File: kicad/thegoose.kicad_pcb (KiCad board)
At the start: 6 copper layers, 88.5 x 47 mm, 190 parts, among them J1 USB_C_Receptacle_USB2.0_16P, J11 Balance, J12 LED stick, J3 XT30UPB-M, J4 USB-A host, J5 IO 3x6 RA, Q1 AO4407A, Q2 80N03F, Q3 80N03F, SW1 Power, SW2 BOOT, U1 DRV8848, U10 RP2354A, U11 SRV05-4, U12 SY6280AAC, U13 BQ7791501, U14 74AHCT1G125, U2 DRV8848, U3 DRV8848, U4 AP64500SP-13, U5 CH224A, U6 SRV05-4, U7 BQ25798, U8 HT7550-1, U9 XC6206P332MR, Y1 12MHz

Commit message: Split into brain + smart pack, and support 2S packs
Brain/pack split: charging, protection and the fuse move off the brain
into a separate smart pack board (kicad-pack/goosepack), with its own
USB-C charging port. The brain drops to 4 layers, loses the charger,
PD sink, protector and SY6280, and swaps the DRV8848s for DRV8871s.

2S support on the brain:
- DRV8871 -> DRV8251A (same HSOP-8 footprint, 4.5-48 V VM). Shared VREF
  divider R107/R108/C81 from +3V3 (2.53 V) and 1.18k IPROPI resistors
  keep the 1.36 A limit.
- Q1 gate divider 27k/10k -> 47k/4.7k for -5.1 V drive at an empty 2S
  pack; C71 4.7n -> 10n to keep the ~70 us soft start.

New 2S pack variant (kicad-pack-2s/goosepack2s): BQ25798 PROG 8.2k
(2S, 750 kHz), ILIM R33 18k (~0.42 A charge), ABLIC S-8252AAH protector
in place of the BQ7791501, two HY2213-BB3A balancers with AO3400A and
47R 2512 bleed resistors, 3-pin XH balance header, R94 4.7k for trip
recovery. fab.py builds it with --board pack2s.

Several new parts still need LCSC numbers; fab.py flags each one.

Co-Authored-By: Claude Opus 5.5 <noreply@anthropic.com>
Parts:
- removed C13, C2, C9: 2.2uF, Capacitor_SMD:C_0603_1608Metric
- removed C17: 1uF, Capacitor_SMD:C_0603_1608Metric
- removed C18, C19: 47nF, Capacitor_SMD:C_0603_1608Metric
- removed C20, C21, C23, C24, C25, C27, C28, C29, C30, C31, C33, C34, C70: 10uF, Capacitor_SMD:C_0805_2012Metric
- removed C22, C26, C32, C60, C68: 100nF, Capacitor_SMD:C_0402_1005Metric
- removed C35: 4.7uF, Capacitor_SMD:C_0603_1608Metric
- removed C36: 1nF, Capacitor_SMD:C_0402_1005Metric
- removed C58, C62, C63, C64, C65, C66, C67: 1uF, Capacitor_SMD:C_0402_1005Metric
- removed D1: SMBJ20A, Diode_SMD:D_SMB
- removed F1: 15A fast, Fuse:Fuse_Littelfuse-NANO2-451_453
- removed J11: Balance, Connector_JST:JST_XH_B4B-XH-A_1x04_P2.50mm_Vertical
- removed L2: 2.2uH, Inductor_SMD:L_Changjiang_FNR4030S
- removed LED1: green, hexy:LED_Everlight_27-21_SideView
- removed Q2, Q3: 80N03F, Package_TO_SOT_SMD:TDSON-8-1
- removed R29, R31, R78: 6.8k, Resistor_SMD:R_0402_1005Metric
- removed R30, R62, R63, R64, R65, R68, R69: 100, Resistor_SMD:R_0402_1005Metric
- removed R32, R50, R76: 100k, Resistor_SMD:R_0402_1005Metric
- removed R33: 33k, Resistor_SMD:R_0402_1005Metric
- removed R34: 5.23k, Resistor_SMD:R_0402_1005Metric
- removed R35: 30.1k, Resistor_SMD:R_0402_1005Metric
- removed R36: 2.2k, Resistor_SMD:R_0402_1005Metric
- removed R37, R38, R39, R54, R75, R77, R79, R81, R85, R89, R93: 10k, Resistor_SMD:R_0402_1005Metric
- removed R61, R72: 1k, Resistor_SMD:R_0402_1005Metric
- removed R66, R67: 5m, Resistor_SMD:R_2512_6332Metric
- removed R70: 4.7k, Resistor_SMD:R_0402_1005Metric
- removed R71, R73: 1M, Resistor_SMD:R_0402_1005Metric
- removed R74: 470k, Resistor_SMD:R_0402_1005Metric
- removed R80: 330, Resistor_SMD:R_0402_1005Metric
- removed R82, R83, R86, R87, R90, R91: 0.15, Resistor_SMD:R_1206_3216Metric
- removed R84, R88, R92: 15k, Resistor_SMD:R_0402_1005Metric
- removed TH1: 10k B3434, Resistor_SMD:R_0603_1608Metric
- removed U12: SY6280AAC, Package_TO_SOT_SMD:SOT-23-5
- removed U13: BQ7791501, Package_SO:TSSOP-24_4.4x7.8mm_P0.65mm
- removed U5: CH224A, Package_SO:SSOP-10-1EP_3.9x4.9mm_P1mm_EP2.1x3.3mm
- removed U7: BQ25798, Package_DFN_QFN:Texas_RQM0029A_VQFN-29_4x4mm_P0.4mm
- added C73: 10uF, Capacitor_SMD:C_0805_2012Metric, F.Cu at (163.6, 122.9)
- added C74: 100nF, Capacitor_SMD:C_0402_1005Metric, F.Cu at (163.3, 121.0)
- added C75: 10uF, Capacitor_SMD:C_0805_2012Metric, F.Cu at (166.4, 121.5)
- added C76: 100nF, Capacitor_SMD:C_0805_2012Metric, F.Cu at (168.5, 121.5)
- added C77: 10uF, Capacitor_SMD:C_0805_2012Metric, F.Cu at (166.4, 138.5)
- added C78: 100nF, Capacitor_SMD:C_0805_2012Metric, F.Cu at (168.5, 138.5)
- added C79: 10uF, Capacitor_SMD:C_0805_2012Metric, F.Cu at (132.0, 108.0)
- added C80: 100nF, Capacitor_SMD:C_0805_2012Metric, F.Cu at (134.0, 108.0)
- added C81: 100nF, Capacitor_SMD:C_0402_1005Metric, F.Cu at (148.0, 152.0)
- added F2: 0.5A hold, Fuse:Fuse_1206_3216Metric, F.Cu at (163.5, 134.0)
- added R100: 5.1k, Resistor_SMD:R_0402_1005Metric, F.Cu at (135.8, 109.8)
- added R101: 1.18k, Resistor_SMD:R_0402_1005Metric, F.Cu at (167.5, 116.2)
- added R102: 1.18k, Resistor_SMD:R_0402_1005Metric, F.Cu at (167.5, 124.7)
- added R103: 1.18k, Resistor_SMD:R_0402_1005Metric, F.Cu at (166.4, 131.0)
- added R104: 1.18k, Resistor_SMD:R_0402_1005Metric, F.Cu at (167.5, 141.7)
- added R105: 1.18k, Resistor_SMD:R_0402_1005Metric, F.Cu at (121.6, 108.7)
- added R106: 1.18k, Resistor_SMD:R_0402_1005Metric, F.Cu at (132.5, 111.8)
- added R107: 10k, Resistor_SMD:R_0402_1005Metric, F.Cu at (140.0, 152.0)
- added R108: 33k, Resistor_SMD:R_0402_1005Metric, F.Cu at (144.0, 152.0)
- added R99: 5.1k, Resistor_SMD:R_0402_1005Metric, F.Cu at (137.2, 109.8)
- added U15: DRV8251A, Package_SO:Texas_HTSOP-8-1EP_3.9x4.9mm_P1.27mm_EP2.95x4.9mm_Mask2.4x3.1mm_ThermalVias, F.Cu at (174.2, 121.5)
- added U16: DRV8251A, Package_SO:Texas_HTSOP-8-1EP_3.9x4.9mm_P1.27mm_EP2.95x4.9mm_Mask2.4x3.1mm_ThermalVias, F.Cu at (174.2, 138.5)
- added U17: DRV8251A, Package_SO:Texas_HTSOP-8-1EP_3.9x4.9mm_P1.27mm_EP2.95x4.9mm_Mask2.4x3.1mm_ThermalVias, F.Cu at (126.5, 109.5)
- C71: value 4.7nF -> 10nF
- R40: value 27k -> 47k
- R41: value 10k -> 4.7k
- U1, U2, U3: value DRV8848 -> DRV8251A; footprint Package_SO:TSSOP-16-1EP_4.4x5mm_P0.65mm -> Package_SO:Texas_HTSOP-8-1EP_3.9x4.9mm_P1.27mm_EP2.95x4.9mm_Mask2.4x3.1mm_ThermalVias
- moved C6 14.5 mm to (167.4, 127.3)
- moved U2 6.89 mm to (174.2, 130.0), turned to 0 degrees
- moved C3 5.91 mm to (166.4, 113.0), turned to 90 degrees
- moved U1 5.69 mm to (174.2, 113.0), turned to 0 degrees
- moved C7 4.90 mm to (168.5, 131.0)
- moved C4 4.70 mm to (168.5, 113.0)
- moved U3 0.94 mm to (114.2, 110.5)
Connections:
- C72 pad 1: VBAT -> PACK+
- J1 pad A5: Net-(J1-CC1) -> /Power/CC1
- J1 pad B5: Net-(J1-CC2) -> /Power/CC2
- J3 pad 1: /Power & charging/BAT_N -> GND
- J3 pad 2: /Power & charging/PACK+ -> PACK+
- M1 pad 1: Net-(M1-OUT1) -> /Motor drivers/U1_OUT1
- M1 pad 2: Net-(M1-OUT2) -> /Motor drivers/U1_OUT2
- M2 pad 1: Net-(M2-OUT1) -> /Motor drivers/U15_OUT2
- M2 pad 2: Net-(M2-OUT2) -> /Motor drivers/U15_OUT1
- M3 pad 1: Net-(M3-OUT1) -> /Motor drivers/U2_OUT1
- M3 pad 2: Net-(M3-OUT2) -> /Motor drivers/U2_OUT2
- M4 pad 1: Net-(M4-OUT1) -> /Motor drivers/U16_OUT2
- M4 pad 2: Net-(M4-OUT2) -> /Motor drivers/U16_OUT1
- M5 pad 1: Net-(M5-OUT1) -> /Motor drivers/U3_OUT1
- M5 pad 2: Net-(M5-OUT2) -> /Motor drivers/U3_OUT2
- M6 pad 1: Net-(M6-OUT1) -> /Motor drivers/U17_OUT2
- M6 pad 2: Net-(M6-OUT2) -> /Motor drivers/U17_OUT1
- Q1 pad 1: VBAT -> PACK+
- Q1 pad 2: VBAT -> PACK+
- Q1 pad 3: VBAT -> PACK+
- R40 pad 1: VBAT -> PACK+
- U1 pad 1: DRV_SLEEP -> /Motor drivers/U1_IPROPI
- U1 pad 2: Net-(M1-OUT1) -> GPIO5_M1B
- U1 pad 3: /Motor drivers/U1_AISEN -> GPIO4_M1A
- U1 pad 4: Net-(M1-OUT2) -> /Motor drivers/MOT_VREF
- U1 pad 5: Net-(M2-OUT1) -> VSYS
- U1 pad 6: /Motor drivers/U1_BISEN -> /Motor drivers/U1_OUT1
- U1 pad 7: Net-(M2-OUT2) -> GND
- U1 pad 8: DRV_FAULT -> /Motor drivers/U1_OUT2
- U1 pad 9: GPIO7_M2A -> GND
- U10 pad 12: I2C_SDA -> unconnected-(U10-GPIO8-Pad12)
- U10 pad 13: CHG_INT -> unconnected-(U10-GPIO9-Pad13)
- U10 pad 28: I2C_SCL -> unconnected-(U10-GPIO17-Pad28)
- U10 pad 31: DRV_FAULT -> unconnected-(U10-GPIO19-Pad31)
- U10 pad 35: DRV_SLEEP -> unconnected-(U10-GPIO23-Pad35)
- U10 pad 37: /MCU & USB/USBA_VBUS_EN -> unconnected-(U10-GPIO25-Pad37)
- U14 pad 4: Net-(R80-Pad1) -> Net-(J12-Pin_2)
- U2 pad 1: DRV_SLEEP -> /Motor drivers/U2_IPROPI
- U2 pad 2: Net-(M3-OUT1) -> GPIO1_M3B
- U2 pad 3: /Motor drivers/U2_AISEN -> GPIO0_M3A
- U2 pad 4: Net-(M3-OUT2) -> /Motor drivers/MOT_VREF
- U2 pad 5: Net-(M4-OUT1) -> VSYS
- U2 pad 6: /Motor drivers/U2_BISEN -> /Motor drivers/U2_OUT1
- U2 pad 7: Net-(M4-OUT2) -> GND
- U2 pad 8: DRV_FAULT -> /Motor drivers/U2_OUT2
- U2 pad 9: GPIO14_M4A -> GND
- U3 pad 1: DRV_SLEEP -> /Motor drivers/U3_IPROPI
- U3 pad 2: Net-(M5-OUT1) -> GPIO11_M5B
- U3 pad 3: /Motor drivers/U3_AISEN -> GPIO10_M5A
- U3 pad 4: Net-(M5-OUT2) -> /Motor drivers/MOT_VREF
- U3 pad 5: Net-(M6-OUT1) -> VSYS
- U3 pad 6: /Motor drivers/U3_BISEN -> /Motor drivers/U3_OUT1
- U3 pad 7: Net-(M6-OUT2) -> GND
- U3 pad 8: DRV_FAULT -> /Motor drivers/U3_OUT2
- U3 pad 9: GPIO13_M6A -> GND
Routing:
- removed copper zone on In3.Cu, net GND
- removed copper zone on In4.Cu, net GND
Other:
- copper layers 6 -> 4
- board text removed: "BAL"
- board text removed: "CHG"
- board text removed: "CHG LED1: side view, lens 0.2 mm behind the top edge at board x 35.83, centre about 0.3 mm above the board; wall hole 1.5 mm"

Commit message: Fill in LCSC numbers, swap to stocked parts, tidy the new schematic parts
- LCSC numbers from JLC's 2026-10-19 in-stock catalog for every new part
  except the DRV8251A, which JLC doesn't stock (Global Sourcing or consign).
- 2S protector S-8252AAH -> HY2120-LB (C168778): pin-for-pin the same,
  OV 4.25 V / UV 2.80 V, stocked at JLC. R94 trip recovery still holds.
- IPROPI R101-R106 1.18k (2,341 in stock) -> 1.2k preferred (C25862),
  so the motor limit is 1.34 A.
- Fix the 2S pack board's footprint-symbol links (paths were dropped in
  the previous commit); both boards now link every footprint correctly.
- Move the VREF divider and the balancer block into clear space and
  rewrite the stale DRV8871/BQ7791501 notes on the motor and 2S sheets.

Co-Authored-By: Claude Opus 5.5 <noreply@anthropic.com>
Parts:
- R101, R102, R103, R104, R105, R106: value 1.18k -> 1.2k

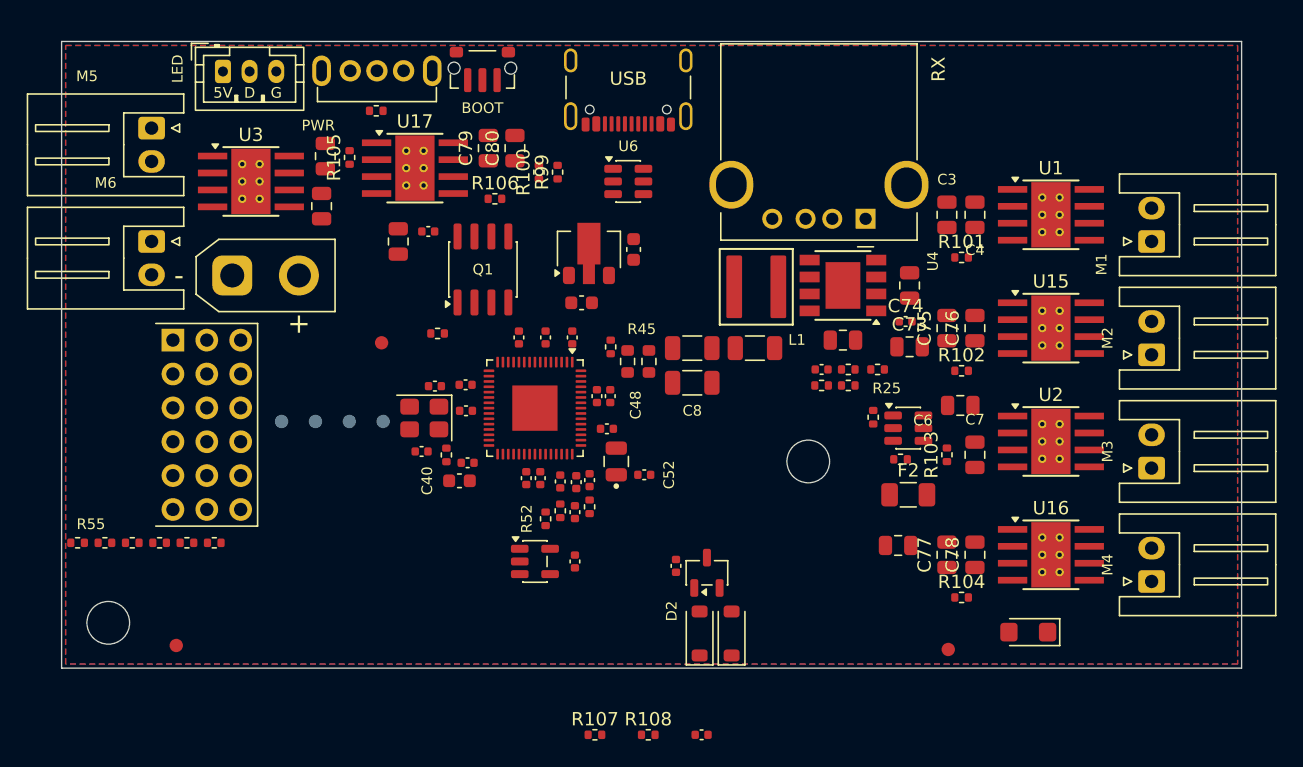
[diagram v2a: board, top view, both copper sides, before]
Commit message: Swap J3 to a horizontal XT30 and compact the brain to 78 x 46.5 mm
- J3: XT30PW-M30.G.Y (C431092) on Connector_AMASS:AMASS_XT30PW-M
  horizontal, bottom edge, mouth out through the wall. Pin 1 PACK-/GND,
  pin 2 PACK+. Hole pattern checked against the Amass drawing.
- Placement compacted from 88.5 x 47 mm to 78 x 46.5 mm (-532.5 mm2,
  -12.8 %; 10.5 mm shorter). Blocks moved as units; edge connectors stay
  on their walls; buck loop and driver-beside-connector kept.
- R107/R108/C81 placed; Edge.Cuts redrawn with 2 mm corners; mounting
  holes, fiducials, GND pours and USB rule areas moved to match.
- Stale pack-envelope and vertical-XT30 fab notes removed or rewritten.
- README/PARTS: new size, placement summary, box = outline + 5 mm.

DRC: no clearance or courtyard errors, no parts outside the outline.

Co-Authored-By: Claude Opus 5.5 <noreply@anthropic.com>
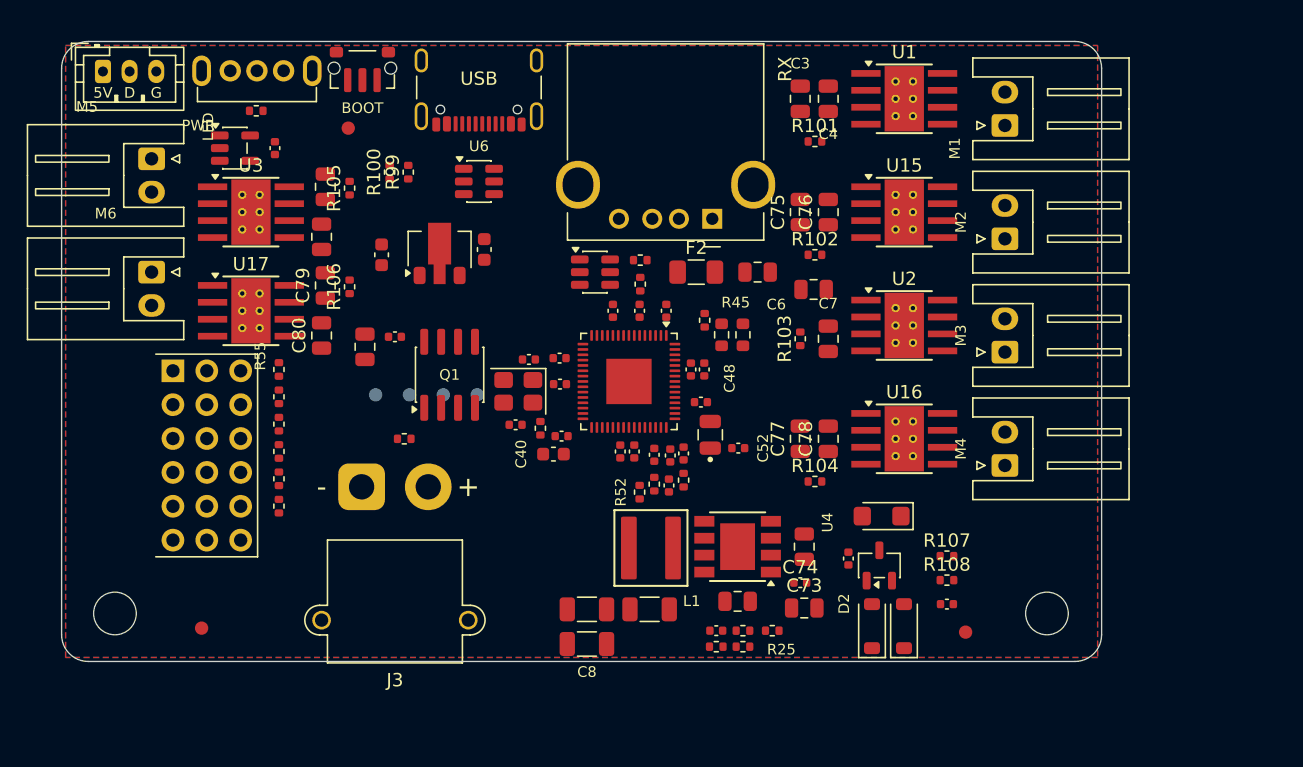
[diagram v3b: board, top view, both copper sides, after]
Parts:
- J3: value XT30UPB-M -> XT30PW-M; footprint hexy:AMASS_XT30UPB-M_1x02_P5.0mm_Vertical_EasyEDA3D -> Connector_AMASS:AMASS_XT30PW-M_1x02_P2.50mm_Horizontal
- moved C69 38.3 mm to (116.0, 108.0)
- moved U14 38.3 mm to (113.0, 108.0)
- moved R107 29.6 mm to (166.4, 138.6)
- moved G*** 26.8 mm to (147.0, 140.5)
- moved U11 26.3 mm to (140.0, 117.3)
- moved R108 25.2 mm to (166.4, 140.4)
- moved R49 23.5 mm to (143.4, 118.2), turned to -90 degrees
- moved F2 23.1 mm to (147.6, 117.3)
- moved C59 23.1 mm to (152.2, 117.3)
- moved REF** 21.2 mm to (173.9, 142.9)
- moved R25 21.1 mm to (153.3, 144.2)
- moved C12 21.1 mm to (144.1, 142.6)
- moved C14 21.1 mm to (150.7, 142.0)
- moved C16 21.1 mm to (149.1, 144.2)
- moved C5 21.1 mm to (139.4, 142.6)
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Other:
- board size 88.5 x 47 mm -> 78 x 46.5 mm
- board text added: "J3 XT30PW-M (male, horizontal) on the bottom edge: the pack's XT30U-F lead plugs in through the bottom wall. Pin 1 PACK- (GND), pin 2 PACK+."
- board text removed: "J3 XT30UPB-M (male, vertical): the pack's XT30U-F plugs in from above; mated + 16 AWG bend 22.1-24.1 mm vs 23.4 under the face (enclosure open item)"
- board text removed: "PACK: Ovonic 80C 3S 450 mAh (standard), envelope 46.5 x 25 x 21 mm (listed 44.1-46 x 24.2-24.7 x 20.3-20.5)"
- board text removed: "mounting hole under the pack: low-profile or nylon wafer head (< 1.5 mm); barrier sheet + foam between pack and board"
- board text removed: "on top of the board, 2.4 mm above it (parts under it <= 1.6 mm, barrier + foam between); leads exit at the left end"

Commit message: Compact the brain further to 73.4 x 43 mm (option B), no mounting holes
- Driver caps and IPROPI resistors moved into a row under each driver,
  next to its VM pin; the motor column moves 4.6 mm left.
- MCU and buck blocks stacked directly under J4; the USB-A strip
  (U11, R48, R49, F2, C59) and the 3.3 V rail (U9, C39, D2, D3) share
  the bottom-right corner. USB-A fan-out rule area moved with U11.
- D4, C15, the VREF divider and FID2 in the column beside J3.
- M3 mounting holes removed; the case holds the board, with a rib
  behind J3 for the plug force.
- 1,003 mm2 (24 %) smaller than the original 88.5 x 47 mm.

DRC: no clearance or courtyard errors, no parts outside the outline,
schematic parity clean.

Co-Authored-By: Claude Opus 5.5 <noreply@anthropic.com>
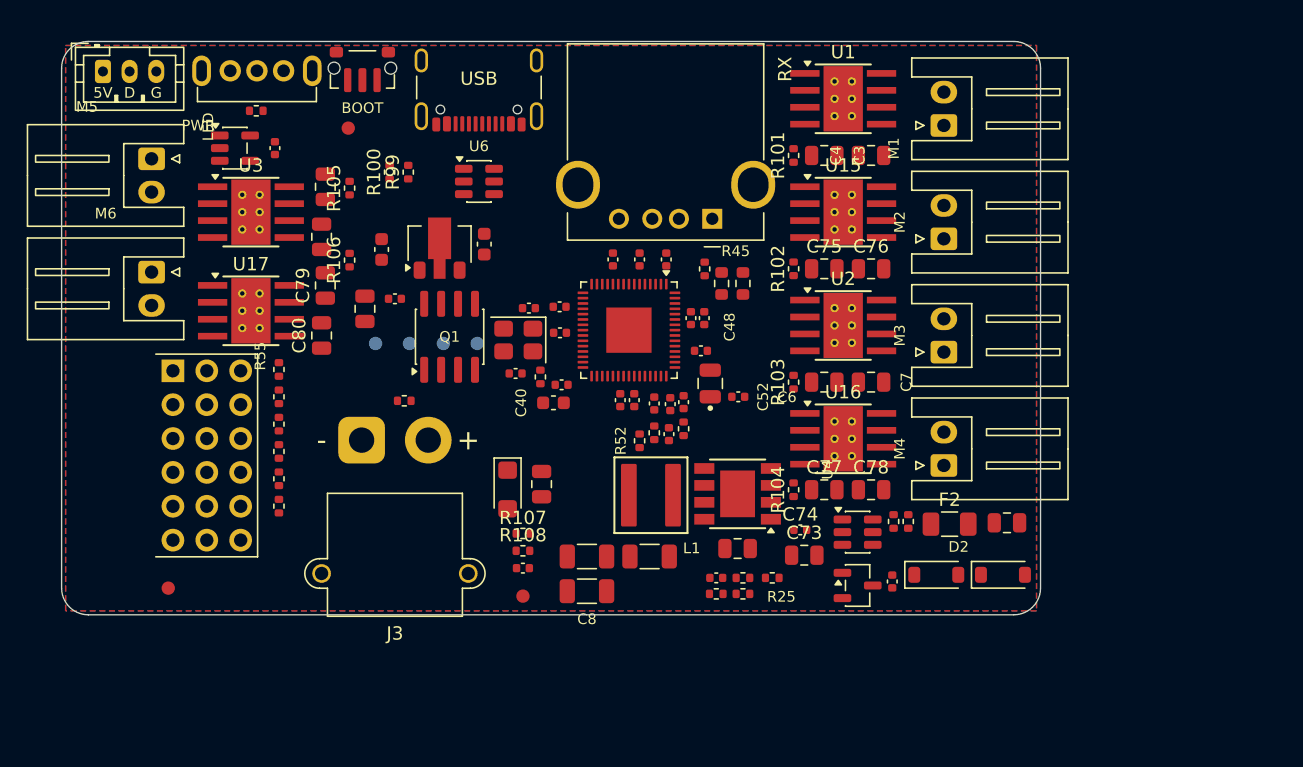
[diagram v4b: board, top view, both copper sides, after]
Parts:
- removed REF** (x2): MountingHole_3.2mm, MountingHole:MountingHole_3.2mm_M3
- moved FID2 33.3 mm to (134.6, 141.6)
- moved C81 31.9 mm to (134.6, 139.5)
- moved R108 31.9 mm to (134.6, 138.2)
- moved R107 31.8 mm to (134.6, 136.9)
- moved D4 28.1 mm to (133.4, 133.6), turned to -90 degrees
- moved U11 27.7 mm to (159.7, 136.8)
- moved R48 27.3 mm to (162.4, 136.0), turned to 90 degrees
- moved R49 26.8 mm to (163.5, 136.0)
- moved F2 26.8 mm to (166.6, 136.2)
- moved C59 26.5 mm to (170.9, 136.1)
- moved C15 20.3 mm to (136.0, 133.2)
- moved D3 8.36 mm to (170.6, 140.0), turned to 0 degrees
- moved C6 7.00 mm to (157.2, 125.5)
- moved D2 6.17 mm to (165.6, 140.0), turned to 0 degrees
- moved C4 5.33 mm to (160.7, 108.5), turned to 0 degrees
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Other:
- board size 78 x 46.5 mm -> 73.4 x 43 mm

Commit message: Baseline before double-sided build
The working tree as handed over: schematics, board, hexy.pretty
footprints and the new STEP models in kicad/3dmodels (now tracked
through a .gitignore exception), plus the double-sided handoff.

Co-Authored-By: Claude Opus 5.5 <noreply@anthropic.com>
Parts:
- moved R99 7.61 mm to (133.5, 108.5), turned to -90 degrees
- moved R100 4.11 mm to (128.5, 108.5), turned to -90 degrees
- turned U17 to 180 degrees
- turned U3 to 180 degrees
- turned U6 to 90 degrees
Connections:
- U15 pad 6: /Motor drivers/U15_OUT1 -> /Motor drivers/U15_OUT2
- U15 pad 8: /Motor drivers/U15_OUT2 -> /Motor drivers/U15_OUT1
- U16 pad 6: /Motor drivers/U16_OUT1 -> /Motor drivers/U16_OUT2
- U16 pad 8: /Motor drivers/U16_OUT2 -> /Motor drivers/U16_OUT1
- U17 pad 6: /Motor drivers/U17_OUT1 -> /Motor drivers/U17_OUT2
- U17 pad 8: /Motor drivers/U17_OUT2 -> /Motor drivers/U17_OUT1
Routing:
- net /Motor drivers/MOT_VREF: track 0.00 -> 106.8 mm, vias 0 -> 3
- net GND: track 0.00 -> 91.0 mm, vias 0 -> 98
- net /MCU & USB/USBA_P: track 0.00 -> 69.4 mm, vias 0 -> 3
- net VCC: track 0.00 -> 60.5 mm, vias 0 -> 4
- net VSYS: track 0.00 -> 52.1 mm, vias 0 -> 34
- net +3V3: track 0.00 -> 45.2 mm, vias 0 -> 22
- net Net-(J4-VBUS): track 0.00 -> 41.1 mm, vias 0 -> 1
- net Net-(R46-Pad2): track 0.00 -> 40.6 mm, vias 0 -> 2
- net Net-(D2-A): track 0.00 -> 40.5 mm, vias 0 -> 2
- net Net-(Q1-G): track 0.00 -> 37.4 mm
- net USB_P: track 0.00 -> 35.5 mm
- net IO6_GPIO: track 0.00 -> 34.8 mm, vias 0 -> 2
- net IO5_GPIO: track 0.00 -> 31.6 mm, vias 0 -> 2
- net USB_N: track 0.00 -> 31.6 mm, vias 0 -> 3
- net VBUS: track 0.00 -> 30.7 mm
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- added copper zone on In2.Cu, net +3V3
- added copper zone on F.Cu, net PACK+
- added copper zone on In2.Cu, net VCC
- added copper zone on In2.Cu, net VSYS
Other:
- board text removed: "BOOT: side push SW2, actuator centre 1.7 mm above the board, flush with the top edge at board x 31.61; case pinhole 3.0-3.2 mm"
- board text removed: "J3 XT30PW-M (male, horizontal) on the bottom edge: the pack's XT30U-F lead plugs in through the bottom wall. Pin 1 PACK- (GND), pin 2 PACK+."
